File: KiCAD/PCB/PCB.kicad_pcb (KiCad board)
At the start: 2 copper layers, 68 x 68 mm, 4 parts, among them J1 XLR3_AudioJack3_Combo_Switch, SW1 RotaryEncoder_Switch, U1 ESP32-WROOM-32D, U2 MPU-6050

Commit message: 原理圖第一版完成
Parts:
- added C1: C, Capacitor_SMD:C_0603_1608Metric, F.Cu at (117.8, 84.8)
- added C2: 10uF, Capacitor_SMD:C_0603_1608Metric, F.Cu at (115.3, 84.8)
- added C3: 470pF, Capacitor_SMD:C_0603_1608Metric, F.Cu at (120.3, 87.8)
- added C4: 2.2uF, Capacitor_SMD:C_0603_1608Metric, F.Cu at (122.8, 83.8)
- added C5: 10nF, Capacitor_SMD:C_0603_1608Metric, F.Cu at (120.3, 83.8)
- added C6: 0.1uF, Capacitor_SMD:C_0603_1608Metric, F.Cu at (115.3, 80.8)
- added J2: Conn_01x04, Connector_PinHeader_1.27mm:PinHeader_1x04_P1.27mm_Vertical, F.Cu at (124.2, 119.6)
- added R1: 4.7K, Resistor_SMD:R_0603_1608Metric, F.Cu at (115.3, 88.8)
- added R2: NC, Resistor_SMD:R_0603_1608Metric, F.Cu at (117.8, 88.8)
- added R3: 4.7K, Resistor_SMD:R_0603_1608Metric, F.Cu at (117.8, 80.8)
- added R4: R, Resistor_SMD:R_0603_1608Metric, F.Cu at (122.8, 87.8)
- added R5: R, Resistor_SMD:R_0603_1608Metric, F.Cu at (117.8, 76.8)
- added R6: R, Resistor_SMD:R_0603_1608Metric, F.Cu at (120.3, 79.8)
- added R7: R, Resistor_SMD:R_0603_1608Metric, F.Cu at (115.3, 76.8)
- added U3: MIC5219-3.3YM5, Package_TO_SOT_SMD:SOT-23-5, F.Cu at (123.4, 92.4)
- moved U2 0.15 mm to (100.0, 113.1)
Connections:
- SW1 pad A: unconnected-(SW1-PadA) -> Net-(SW1-PadA)
- SW1 pad B: unconnected-(SW1-PadB) -> Net-(SW1-PadB)
- SW1 pad C: unconnected-(SW1-PadC) -> Net-(SW1-PadC)
- SW1 pad S1: unconnected-(SW1-PadS1) -> /3V3
- SW1 pad S2: unconnected-(SW1-PadS2) -> Net-(SW1-PadS2)
- U1 pad 10: unconnected-(U1-Pad10) -> /ENCODER_B
- U1 pad 2: unconnected-(U1-Pad2) -> /3V3
- U1 pad 25: unconnected-(U1-Pad25) -> /MPU_INT
- U1 pad 33: unconnected-(U1-Pad33) -> /SDA
- U1 pad 34: unconnected-(U1-Pad34) -> /UART_RX
- U1 pad 35: unconnected-(U1-Pad35) -> /UART_TX
- U1 pad 36: unconnected-(U1-Pad36) -> /SCL
- U1 pad 8: unconnected-(U1-Pad8) -> /ENCODER_C
- U1 pad 9: unconnected-(U1-Pad9) -> /ENCODER_A
- U2 pad 12: unconnected-(U2-Pad12) -> /MPU_INT
- U2 pad 13: unconnected-(U2-Pad13) -> /3V3
- U2 pad 18: unconnected-(U2-Pad18) -> GND
- U2 pad 23: unconnected-(U2-Pad23) -> /SCL
- U2 pad 24: unconnected-(U2-Pad24) -> /SDA
- U2 pad 8: unconnected-(U2-Pad8) -> /3V3
- U2 pad 9: unconnected-(U2-Pad9) -> Net-(U2-Pad9)

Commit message: 完成佈件
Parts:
- added C1: 22p, Capacitor_SMD:C_0603_1608Metric, F.Cu at (106.1, 119.6)
- added C10: 0.1uF, Capacitor_SMD:C_0603_1608Metric, F.Cu at (116.6, 125.7)
- added C11: 0.1uF, Capacitor_SMD:C_0603_1608Metric, F.Cu at (86.6, 125.7)
- added C12: 0.1uF, Capacitor_SMD:C_0603_1608Metric, F.Cu at (119.9, 79.5)
- added C14: 0.1uF, Capacitor_SMD:C_0603_1608Metric, F.Cu at (73.7, 83.1)
- added C3: 22p, Capacitor_SMD:C_0603_1608Metric, F.Cu at (106.0, 123.0)
- added C6: 4.7uF, Capacitor_SMD:C_0603_1608Metric, F.Cu at (92.2, 117.3)
- added C8: 4.7uF, Capacitor_SMD:C_0603_1608Metric, F.Cu at (80.4, 113.0)
- added C9: 100pF, Capacitor_SMD:C_0603_1608Metric, F.Cu at (77.0, 112.9)
- added D1: D, Diode_SMD:D_SOD-323, F.Cu at (80.3, 118.3)
- added D2: D, Diode_SMD:D_SOD-323, F.Cu at (80.3, 115.8)
- added D3: LED, LED_SMD:LED_0201_0603Metric, F.Cu at (113.1, 72.8)
- added D4: LED, LED_SMD:LED_0201_0603Metric, F.Cu at (85.5, 102.3)
- added D5: LED, LED_SMD:LED_0201_0603Metric, F.Cu at (88.2, 117.8)
- added J2: Conn_01x02, Connector_PinHeader_1.00mm:PinHeader_1x02_P1.00mm_Horizontal, F.Cu at (77.3, 115.8)
- added P1: USB_C_Plug, Connector_USB:HRI_TYPE_C, F.Cu at (99.2, 132.1)
- added Q1: Q_NPN_EBC, Package_TO_SOT_SMD:SOT-23, F.Cu at (101.3, 111.0)
- added Q2: Q_NPN_EBC, Package_TO_SOT_SMD:SOT-23, F.Cu at (97.3, 111.0)
- added R10: 4.7K, Resistor_SMD:R_0402_1005Metric, F.Cu at (96.8, 95.5)
- added R11: 470R, Resistor_SMD:R_0402_1005Metric, F.Cu at (113.3, 70.4)
- added R12: 1M, Resistor_SMD:R_0402_1005Metric, F.Cu at (79.8, 110.7)
- added R13: 10K, Resistor_SMD:R_0402_1005Metric, F.Cu at (117.1, 116.5)
- added R14: 1MR, Resistor_SMD:R_0402_1005Metric, F.Cu at (79.8, 111.6)
- added R18: 470R, Resistor_SMD:R_0402_1005Metric, F.Cu at (94.8, 109.8)
- added R19: 10K, Resistor_SMD:R_0402_1005Metric, F.Cu at (90.2, 126.2)
- added R2: R, Resistor_SMD:R_0402_1005Metric, F.Cu at (96.8, 113.7)
- added R22: 330R, Resistor_SMD:R_0402_1005Metric, F.Cu at (93.0, 70.1)
- added R23: 4.7K, Resistor_SMD:R_0402_1005Metric, F.Cu at (119.4, 78.0)
- added R24: 330R, Resistor_SMD:R_0402_1005Metric, F.Cu at (106.3, 93.5)
- added R25: 4.7K, Resistor_SMD:R_0402_1005Metric, F.Cu at (73.2, 81.5)
- added R4: 1K, Resistor_SMD:R_0402_1005Metric, F.Cu at (95.5, 70.1)
- added R5: R, Resistor_SMD:R_0402_1005Metric, F.Cu at (115.2, 72.7)
- added R6: R, Resistor_SMD:R_0402_1005Metric, F.Cu at (86.8, 102.4)
- added R7: 2K, Resistor_SMD:R_0402_1005Metric, F.Cu at (84.8, 121.5)
- added R8: 470R, Resistor_SMD:R_0402_1005Metric, F.Cu at (85.2, 118.0)
- added R9: 4.7K, Resistor_SMD:R_0402_1005Metric, F.Cu at (95.8, 95.5)
- added SW1: SW_Push, Button_Switch_SMD:SW_Push_SPST_NO_Alps_SKRK, F.Cu at (116.5, 120.1)
- added SW2: SW_Push, Button_Switch_SMD:SW_Push_SPST_NO_Alps_SKRK, F.Cu at (89.9, 128.8)
- added SW4: SW_Push, Button_Switch_SMD:SW_SPST_EVQP7C, F.Cu at (122.0, 76.3)
- added SW5: SW_Push, Button_Switch_SMD:SW_SPST_EVQP7C, F.Cu at (76.7, 77.5)
- added U2: CH340G, Package_SO:SOIC-16_3.9x9.9mm_P1.27mm, F.Cu at (98.5, 119.5)
- added U3: MCP73832-5-OT, Package_TO_SOT_SMD:SOT-23-5, F.Cu at (88.0, 121.1)
- added Y1: 12Mhz, Crystal:Crystal_SMD_HC49-SD, F.Cu at (109.8, 122.8)
- C2: renamed from C1; value C -> 4.7uF
- J1: value XLR3_AudioJack3_Combo_Switch -> Conn_01x04; footprint Button_Switch_THT:SW_E-Switch_EG2219_DPDT_Angled -> Connector_PinHeader_1.00mm:PinHeader_1x04_P1.00mm_Horizontal; moved to B.Cu
- R1: value 4.7K -> R; footprint Resistor_SMD:R_0603_1608Metric -> Resistor_SMD:R_0402_1005Metric
- R15: renamed from R4; footprint Resistor_SMD:R_0603_1608Metric -> Resistor_SMD:R_0402_1005Metric
- R16: renamed from R5; footprint Resistor_SMD:R_0603_1608Metric -> Resistor_SMD:R_0402_1005Metric
- R17: renamed from R6; footprint Resistor_SMD:R_0603_1608Metric -> Resistor_SMD:R_0402_1005Metric
- R20: renamed from R7; value R -> 10KR; footprint Resistor_SMD:R_0603_1608Metric -> Resistor_SMD:R_0402_1005Metric
- R21: renamed from R2; footprint Resistor_SMD:R_0603_1608Metric -> Resistor_SMD:R_0402_1005Metric
- R3: footprint Resistor_SMD:R_0603_1608Metric -> Resistor_SMD:R_0402_1005Metric
- moved J1 53.9 mm to (101.1, 68.0), turned to -90 degrees
- moved C5 47.1 mm to (81.7, 106.8)
- moved U1 40.9 mm to (85.0, 106.6), turned to 180 degrees
- moved C4 39.2 mm to (84.5, 103.8), turned to 0 degrees
- moved C2 36.9 mm to (88.2, 107.0)
- moved R1 29.7 mm to (99.1, 113.7), turned to 180 degrees
- moved C13 29.6 mm to (92.1, 92.9), turned to 180 degrees
- moved R20 26.7 mm to (110.5, 103.0)
- moved R21 24.3 mm to (98.6, 103.8), turned to 180 degrees
- moved R3 23.7 mm to (96.6, 70.1)
- moved R17 22.6 mm to (102.3, 93.5)
- moved C15 21.9 mm to (103.8, 99.4)
- moved C7 21.3 mm to (103.8, 102.7)
- moved R16 21.1 mm to (105.0, 93.5)
- moved R15 20.0 mm to (103.7, 93.5)
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- renumbered C5 to C13, C6 to C15, C3 to C4, C4 to C5, C2 to C7, J2 to LCD1, SW1 to SW3, U3 to U1, U1 to U4, U2 to U5
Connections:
- net /5V renamed Net-(C2-Pad1)
- C13 pad 1: /3V3 -> +3V3
- C15 pad 1: /3V3 -> +3V3
- C5 pad 1: /3V3 -> +3V3
- C7 pad 1: unconnected-(C2-Pad1) -> +3V3
- C7 pad 2: unconnected-(C2-Pad2) -> GND
- J1 pad 1: unconnected-(J1-Pad1) -> +5V
- J1 pad 2: unconnected-(J1-Pad2) -> /UART_RX
- J1 pad 3: unconnected-(J1-Pad3) -> /UART_TX
- J1 pad 4: (no net) -> GND
- LCD1 pad 1: unconnected-(J2-Pad1) -> /3V3
- LCD1 pad 2: unconnected-(J2-Pad2) -> GND
- LCD1 pad 3: unconnected-(J2-Pad3) -> /LCD_SCL
- LCD1 pad 4: unconnected-(J2-Pad4) -> /LCD_SDA
- R1 pad 1: +3V3 -> /DTR
- R1 pad 2: /SDA -> Net-(Q2-Pad2)
- R3 pad 1: +3V3 -> Net-(R3-Pad1)
- R3 pad 2: /SCL -> /UART_RX
- U1 pad 5: /3V3 -> +3V3
- U4 pad 1: Net-(U1-Pad1) -> GND
- U4 pad 11: unconnected-(U1-Pad11) -> /BT2
- U4 pad 15: Net-(U1-Pad1) -> GND
- U4 pad 2: /3V3 -> +3V3
- U4 pad 24: unconnected-(U1-Pad24) -> /ESP32_IO2
- U4 pad 25: /MPU_INT -> /ESP32_IO0
- U4 pad 26: unconnected-(U1-Pad26) -> /ADC0
- U4 pad 3: unconnected-(U1-Pad3) -> /ESP32_EN
- U4 pad 31: unconnected-(U1-Pad31) -> /MPU_INT
- U4 pad 33: /SDA -> /LCD_SDA
- U4 pad 36: /SCL -> /LCD_SCL
- U4 pad 37: unconnected-(U1-Pad37) -> /BT1
- U4 pad 38: Net-(U1-Pad1) -> GND
- U4 pad 39: Net-(U1-Pad1) -> GND
- U5 pad 13: /3V3 -> +3V3
- U5 pad 23: /SCL -> /LCD_SCL
- U5 pad 24: /SDA -> /LCD_SDA
- U5 pad 8: /3V3 -> +3V3

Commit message: 完成佈線
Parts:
- added V0.1: LOGO, LOGO, B.Cu at (101.0, 82.5)
- moved D1 13.0 mm to (92.7, 114.6), turned to -90 degrees
- moved R11 5.35 mm to (108.0, 70.4), turned to 90 degrees
- moved R13 4.26 mm to (115.8, 120.5)
- moved SW1 4.06 mm to (116.5, 124.2)
- moved SW4 3.98 mm to (125.0, 79.0)
- moved R19 3.95 mm to (93.0, 123.4), turned to -90 degrees
- moved R5 3.73 mm to (115.3, 76.5)
- moved D3 3.62 mm to (113.0, 76.5)
- moved C11 3.32 mm to (89.9, 126.0)
- moved R25 3.21 mm to (76.2, 82.5), turned to 180 degrees
- moved C10 3.18 mm to (119.4, 124.2), turned to 90 degrees
- moved R20 2.64 mm to (109.5, 100.6)
- moved SW5 2.29 mm to (75.0, 79.0)
- moved R7 2.17 mm to (85.1, 119.4)
- moved C14 2.05 mm to (75.4, 84.1)
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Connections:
- LCD1 pad 1: /3V3 -> +3V3
- SW3 pad S1: /3V3 -> +3V3
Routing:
- net +3V3: track 0.00 -> 254.5 mm, vias 0 -> 9
- net +5V: track 0.00 -> 106.9 mm, vias 0 -> 2
- net /LCD_SDA: track 0.00 -> 86.4 mm, vias 0 -> 3
- net /LCD_SCL: track 0.00 -> 85.9 mm, vias 0 -> 3
- net Net-(C10-Pad2): track 0.00 -> 80.1 mm
- net Net-(R3-Pad1): track 0.00 -> 65.7 mm, vias 0 -> 2
- net Net-(R4-Pad1): track 0.00 -> 64.7 mm, vias 0 -> 2
- net /ADC0: track 0.00 -> 63.1 mm
- net Net-(C14-Pad2): track 0.00 -> 47.7 mm, vias 0 -> 2
- net /ESP32_IO0: track 0.00 -> 46.4 mm
- net /MPU_INT: track 0.00 -> 46.0 mm, vias 0 -> 4
- net Net-(C12-Pad2): track 0.00 -> 44.1 mm
- net GND: track 0.00 -> 42.2 mm, vias 0 -> 88
- net Net-(C2-Pad1): track 0.00 -> 30.9 mm
- net Net-(C11-Pad2): track 0.00 -> 25.1 mm, vias 0 -> 2
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- added copper zone on B.Cu, net GND
- added copper zone on F.Cu, net GND
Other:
- board text added: "X"
- board text added: "Y"
- board text added: "Z"
- board text added: "https://github.com/Oliver0804/ESP32_SpaceRat"

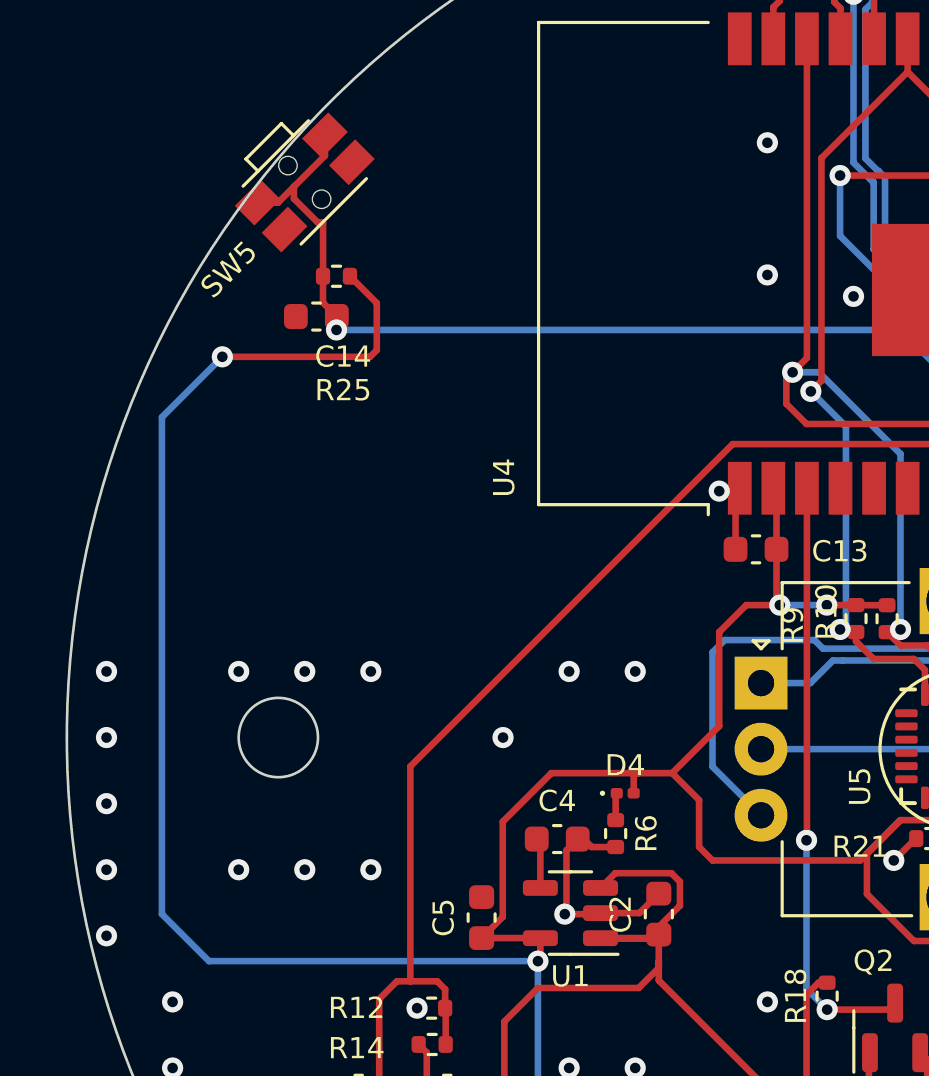
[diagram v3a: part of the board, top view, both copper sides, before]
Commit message: 更新第二版原理圖
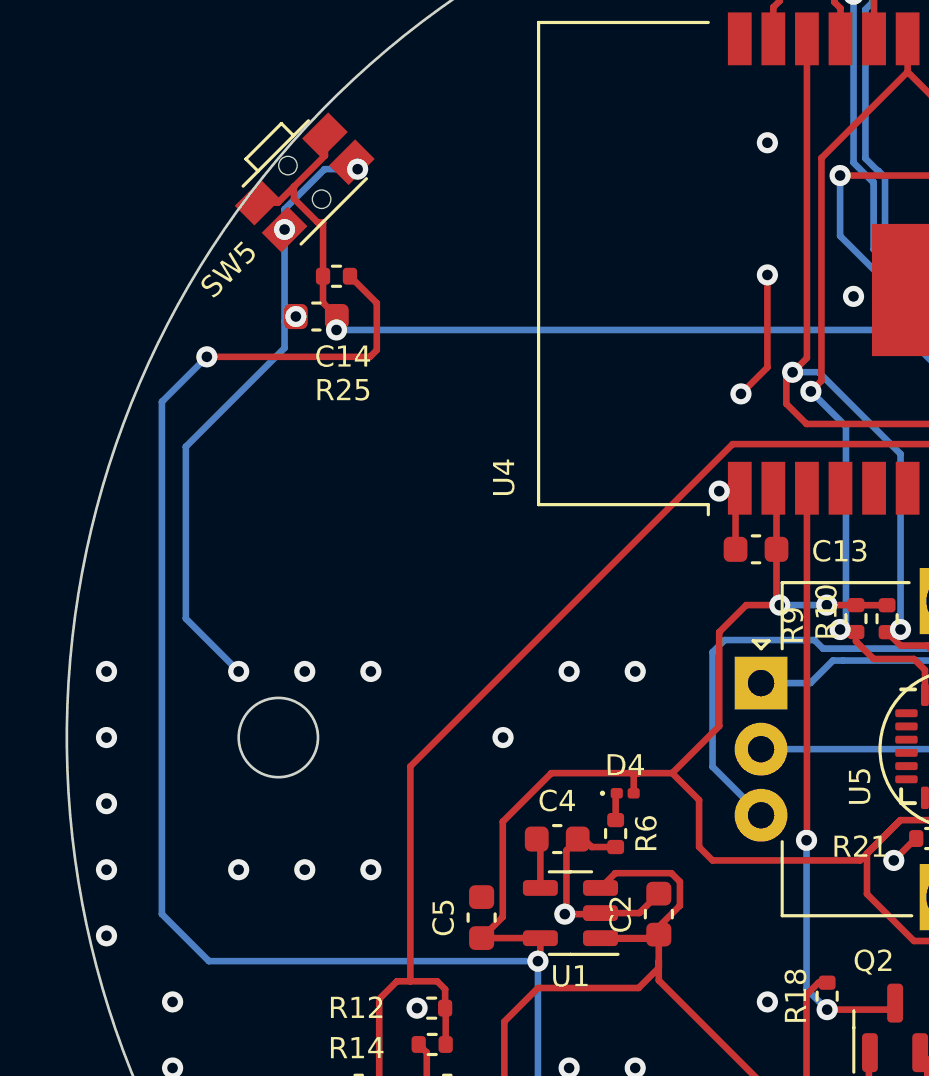
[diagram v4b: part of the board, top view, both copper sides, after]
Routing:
- net GND: track 42.2 -> 71.2 mm, vias 88 -> 92
